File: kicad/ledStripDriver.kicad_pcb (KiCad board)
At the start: 2 copper layers, 110 x 91 mm, 33 parts, among them J1 AudioJack3_SwitchTR, K1 G5RL1AELN5DC, Q1 Q_NPN_BEC_S8050, Q2 AO3400, Q3 AO3400, Q4 AO3400, SW1 SW_DIP_x01, SW2 Rotary_Encoder_Switch, SW3 SW_Push, U1 MOD_ESP32_DEV_universal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

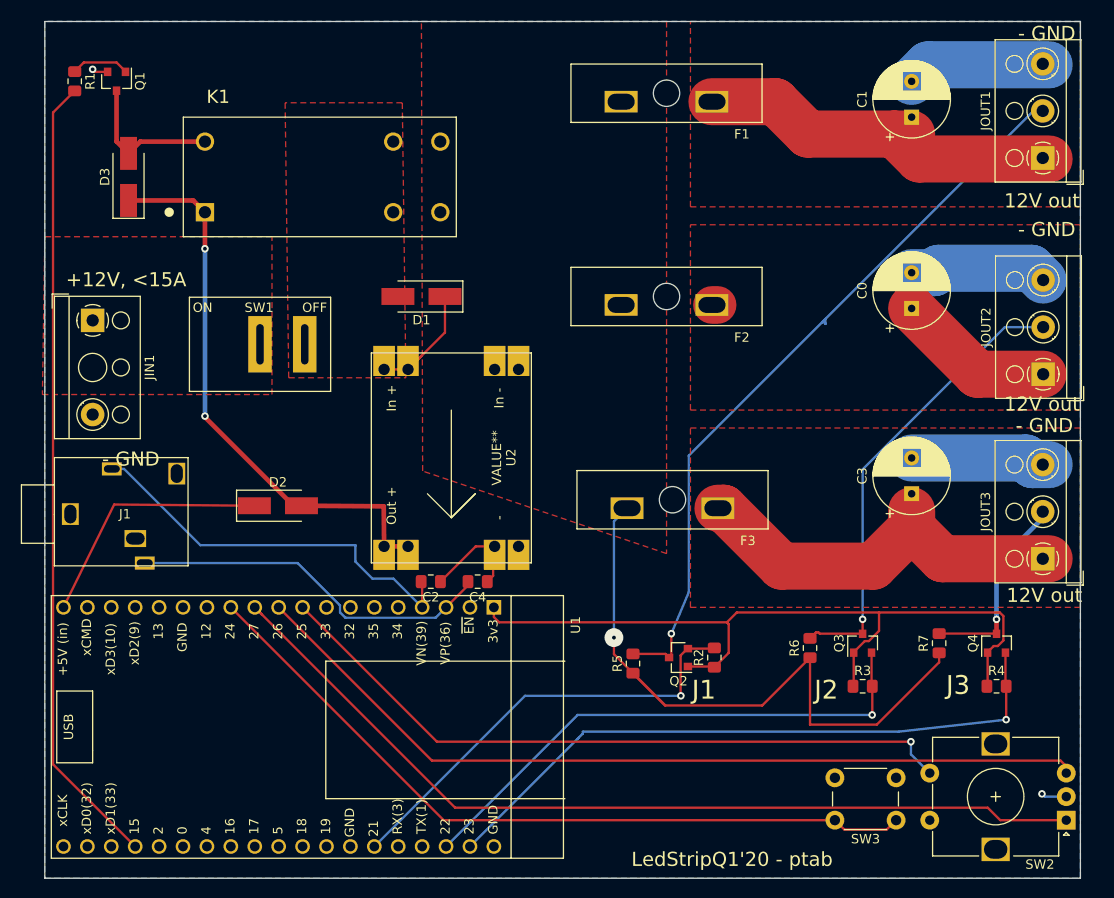
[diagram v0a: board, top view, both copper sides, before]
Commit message: KiCad fixes: flip Jack, add resistor on 12V logic to protect LEDs.
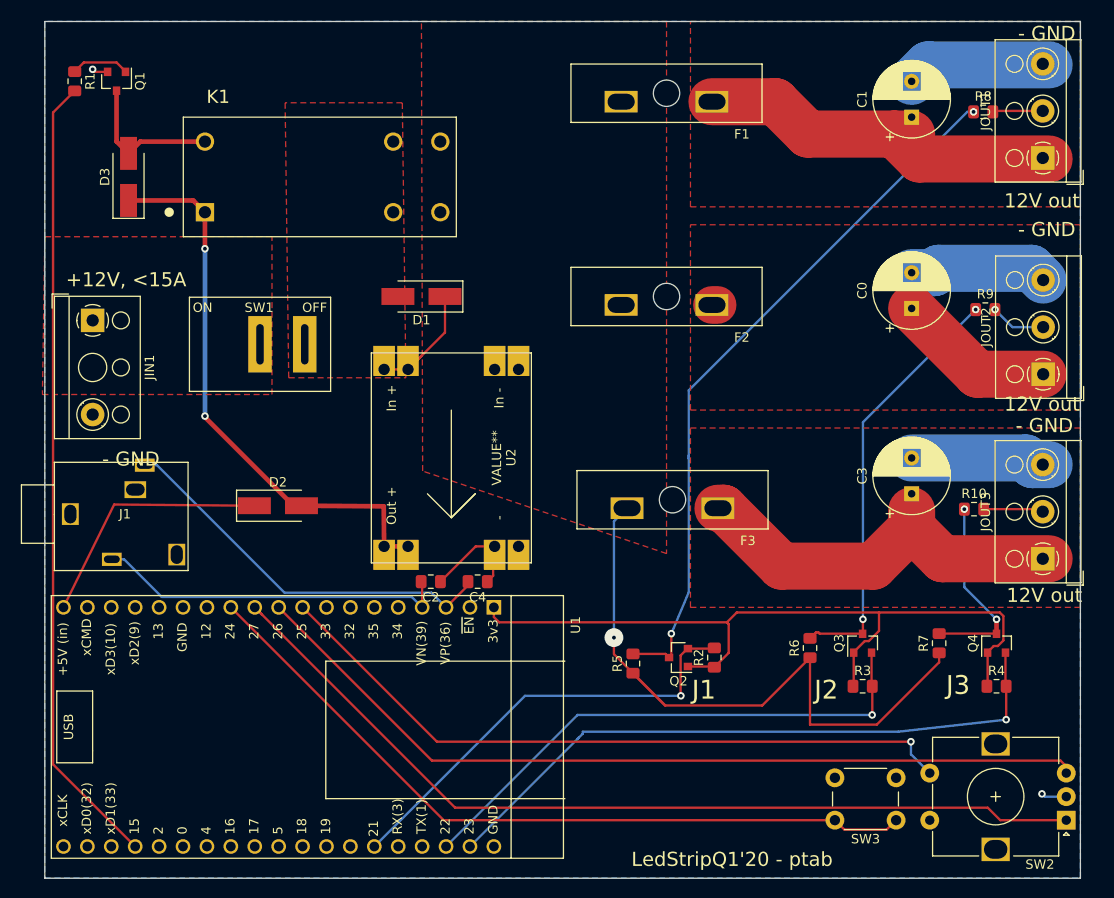
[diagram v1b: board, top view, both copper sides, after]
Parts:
- added R10: 300ohm, Resistor_SMD:R_0805_2012Metric_Pad1.15x1.40mm_HandSolder, F.Cu at (198.7, 101.8)
- added R8: 300ohm, Resistor_SMD:R_0805_2012Metric_Pad1.15x1.40mm_HandSolder, F.Cu at (199.7, 59.6)
- added R9: 300ohm, Resistor_SMD:R_0805_2012Metric_Pad1.15x1.40mm_HandSolder, F.Cu at (199.9, 80.6)
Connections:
- Q2 pad 3: /STRIP1_LOGIC_12V -> Net-(Q2-Pad3)
- Q3 pad 3: /STRIP2_LOGIC_12V -> Net-(Q3-Pad3)
- Q4 pad 3: /STRIP3_LOGIC_12V -> Net-(Q4-Pad3)
- R5 pad 2: /STRIP1_LOGIC_12V -> Net-(Q2-Pad3)
- R6 pad 2: /STRIP2_LOGIC_12V -> Net-(Q3-Pad3)
- R7 pad 2: /STRIP3_LOGIC_12V -> Net-(Q4-Pad3)
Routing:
- net Net-(Q2-Pad3): track 0.00 -> 75.6 mm, vias 0 -> 2
- net /STRIP1_LOGIC_12V: track 80.7 -> 7.11 mm, vias 1 -> 0
- net Net-(Q3-Pad3): track 0.00 -> 45.3 mm, vias 0 -> 2
- net /STRIP2_LOGIC_12V: track 48.8 -> 5.89 mm
- net Net-(Q4-Pad3): track 0.00 -> 20.8 mm, vias 0 -> 2
- net /STRIP3_LOGIC_12V: track 21.4 -> 6.39 mm, vias 1 -> 0
- net Net-(C2-Pad2): track 42.9 -> 37.9 mm
- net Net-(C4-Pad2): track 39.0 -> 42.0 mm

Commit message: Refreshed PCB and footprints of (Fuse holder, Rocker switch, Screw-terminal for input)
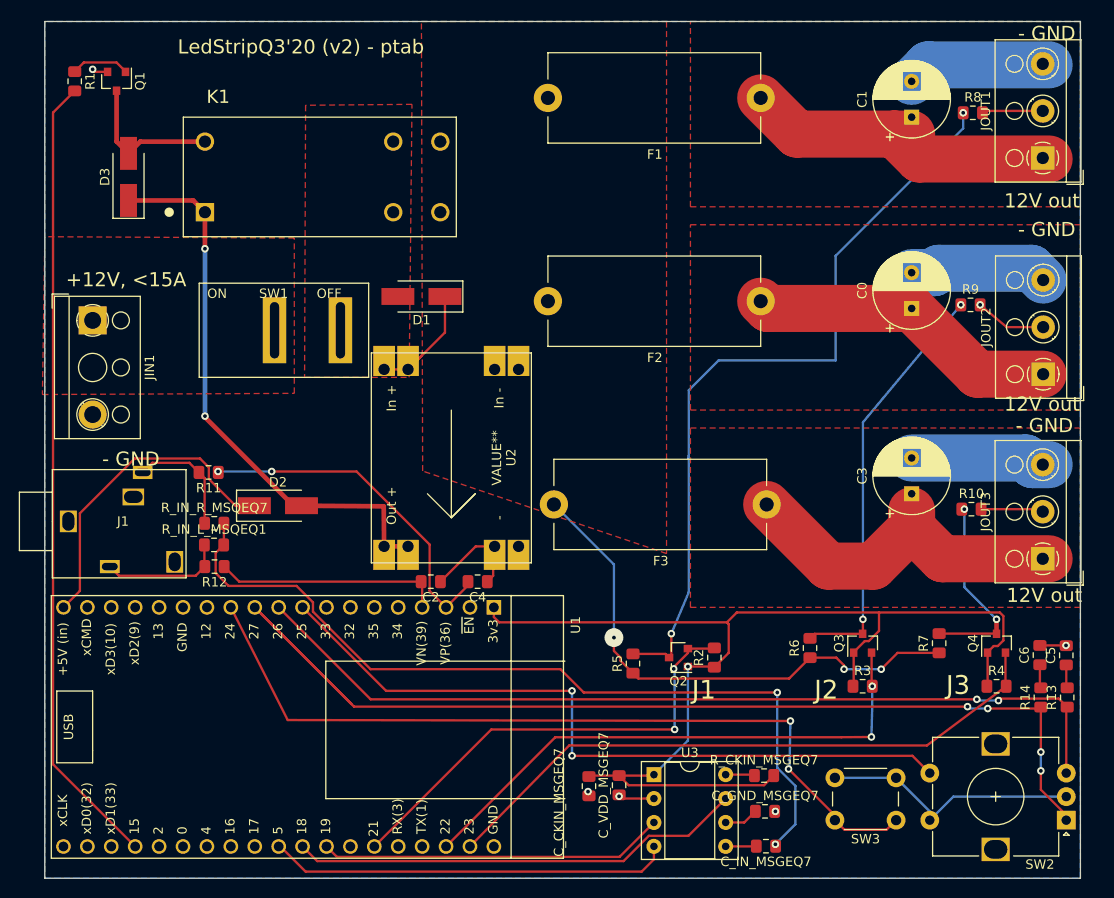
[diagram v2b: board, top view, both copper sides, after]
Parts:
- added C5: 10nF, Capacitor_SMD:C_0805_2012Metric_Pad1.15x1.40mm_HandSolder, F.Cu at (208.5, 117.3)
- added C6: 10nF, Capacitor_SMD:C_0805_2012Metric_Pad1.15x1.40mm_HandSolder, F.Cu at (205.7, 117.3)
- added C_CKIN_MSGEQ7: 33pF, Capacitor_SMD:C_0805_2012Metric_Pad1.15x1.40mm_HandSolder, F.Cu at (157.8, 131.2)
- added C_GND_MSGEQ7: 0.1uF, Capacitor_SMD:C_0805_2012Metric_Pad1.15x1.40mm_HandSolder, F.Cu at (176.5, 133.9)
- added C_IN_MSGEQ7: 10nF, Capacitor_SMD:C_0805_2012Metric_Pad1.15x1.40mm_HandSolder, F.Cu at (176.6, 137.6)
- added C_VDD_MSGEQ7: 0.1uF, Capacitor_SMD:C_0805_2012Metric_Pad1.15x1.40mm_HandSolder, F.Cu at (161.0, 131.1)
- added R11: R, Resistor_SMD:R_0805_2012Metric_Pad1.15x1.40mm_HandSolder, F.Cu at (117.4, 97.9)
- added R12: R, Resistor_SMD:R_0805_2012Metric_Pad1.15x1.40mm_HandSolder, F.Cu at (118.0, 107.9)
- added R13: 10k, Resistor_SMD:R_0805_2012Metric_Pad1.15x1.40mm_HandSolder, F.Cu at (208.6, 121.8)
- added R14: 10k, Resistor_SMD:R_0805_2012Metric_Pad1.15x1.40mm_HandSolder, F.Cu at (205.8, 121.8)
- added R_CKIN_MSGEQ7: 200k, Resistor_SMD:R_0805_2012Metric_Pad1.15x1.40mm_HandSolder, F.Cu at (176.4, 130.1)
- added R_IN_L_MSQEQ1: 22k, Resistor_SMD:R_0805_2012Metric_Pad1.15x1.40mm_HandSolder, F.Cu at (118.0, 105.6)
- added R_IN_R_MSQEQ7: 22k, Resistor_SMD:R_0805_2012Metric_Pad1.15x1.40mm_HandSolder, F.Cu at (118.0, 103.3)
- added U3: MSGEQ7, Package_DIP:DIP-8_W7.62mm_Socket, F.Cu at (164.7, 130.0)
- F1, F2, F3: footprint ptabOther:FUSE_HOLDER_CAR_MEDIUM_PA66 -> Fuse:Fuseholder_Cylinder-5x20mm_Stelvio-Kontek_PTF78_Horizontal_Open
- JIN1: footprint TerminalBlock_RND:TerminalBlock_RND_205-00023_1x02_P10.00mm_Horizontal -> ptabOther:TerminalBlock_RND_205-00023_1x02_P10.00mm_Horizontal(2mmdrill)
- SW1: footprint ptabOther:ROCKER_SWITCH -> ptabOther:ROCKER_SWITCH_7x0.5mm
- moved F1 10.0 mm to (176.0, 58.1)
- moved F2 10.0 mm to (176.0, 79.7)
- moved F3 10.0 mm to (176.7, 101.3)
- moved SW1 2.14 mm to (124.4, 82.8)
- moved R9 1.65 mm to (198.3, 80.1)
- moved R8 1.10 mm to (198.6, 59.7)
- moved J1 0.81 mm to (100.8, 103.1)
- moved R10 0.27 mm to (198.4, 101.8)
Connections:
- net Net-(D2-Pad1) renamed /VDD_5V
- J1 pad R: Net-(C4-Pad2) -> Net-(J1-PadR)
- J1 pad T: Net-(C2-Pad2) -> Net-(J1-PadT)
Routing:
- net Net-(C_IN_MSGEQ7-Pad1): track 0.00 -> 88.9 mm, vias 0 -> 2
- net Net-(U1-Pad28): track 0.00 -> 48.3 mm
- net Net-(U1-Pad29): track 0.00 -> 42.9 mm
- net +3V3: track 82.0 -> 119.2 mm, vias 0 -> 1
- net Net-(U1-Pad27): track 0.00 -> 36.8 mm
- net GND: track 61.4 -> 92.7 mm, vias 2 -> 5
- net Net-(R14-Pad1): track 97.4 -> 115.7 mm, vias 0 -> 4
- net /12V_JOUT2: track 17.5 -> 33.2 mm
- net /12V_POST_RELAY: track 70.7 -> 56.5 mm, vias 1 -> 3
- net Net-(C2-Pad2): track 37.9 -> 24.4 mm
- net Net-(J1-PadT): track 0.00 -> 13.2 mm
- net Net-(J1-PadR): track 0.00 -> 12.5 mm
- net /VDD_5V: track 27.1 -> 34.5 mm
- net Net-(Q2-Pad3): track 75.6 -> 82.0 mm
- net Net-(SW3-Pad1): track 80.9 -> 86.8 mm, vias 0 -> 2
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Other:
- board text added: "LedStripQ3'20 (v2) - ptab"
- board text removed: "LedStripQ1'20 - ptab"

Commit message: PCB v2 - with hardware spectrum analyzer.
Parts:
- moved SW3 7.75 mm to (184.0, 130.5), turned to 0 degrees
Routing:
- net Net-(SW3-Pad1): track 86.8 -> 75.1 mm
- net GND: track 92.7 -> 91.6 mm

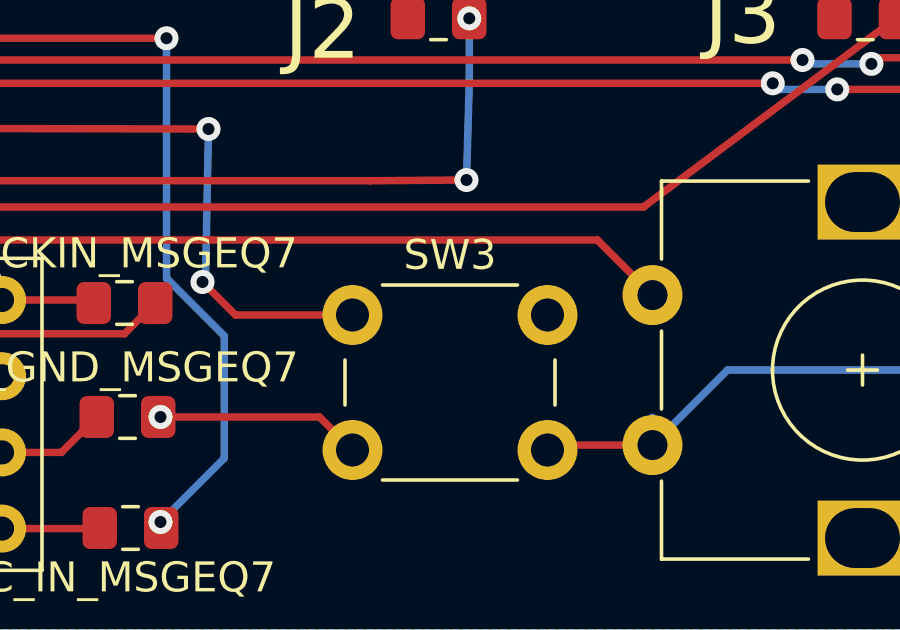
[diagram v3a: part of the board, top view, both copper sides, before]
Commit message: Revision 2 - Q3'2020 -> Printed board (rev2), Software confirmed to work. No support for Jack yet.
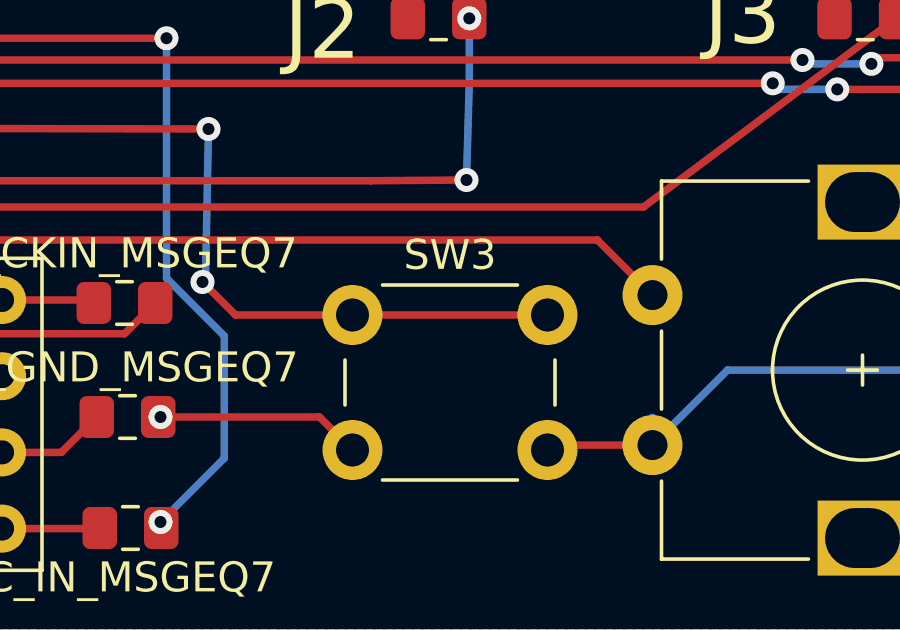
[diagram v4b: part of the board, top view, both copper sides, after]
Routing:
- net Net-(SW3-Pad1): track 75.1 -> 81.6 mm
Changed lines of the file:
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@@
   (general
     (thickness 1.6)
-    (drawings 19)
-    (tracks 307)
+    (drawings 16)
+    (tracks 308)
     (zones 0)
     (modules 50)
@@
     (effects (font (size 2 2) (thickness 0.15)))
   )
-  (target plus (at 210 50) (size 5) (width 0.05) (layer Edge.Cuts))
-  (target plus (at 100 141) (size 5) (width 0.05) (layer Edge.Cuts))
-  (target plus (at 210 141) (size 5) (width 0.05) (layer Edge.Cuts))
   (gr_line (start 210 50) (end 100 50) (layer Edge.Cuts) (width 0.05))
   (gr_line (start 210 141) (end 210 50) (layer Edge.Cuts) (width 0.05))
@@
   (segment (start 180.1 130.5) (end 179 129.4) (width 0.25) (layer F.Cu) (net 50))
   (segment (start 184 130.5) (end 180.1 130.5) (width 0.25) (layer F.Cu) (net 50))
+  (segment (start 184 130.5) (end 190.5 130.5) (width 0.25) (layer F.Cu) (net 50))
   (segment (start 140.08 109.605) (end 139.975 109.5) (width 0.25) (layer F.Cu) (net 51) (status 30))
   (segment (start 140.08 112.23) (end 140.08 109.605) (width 0.25) (layer F.Cu) (net 51) (status 30))
